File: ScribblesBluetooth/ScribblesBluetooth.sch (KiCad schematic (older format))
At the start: 9 parts

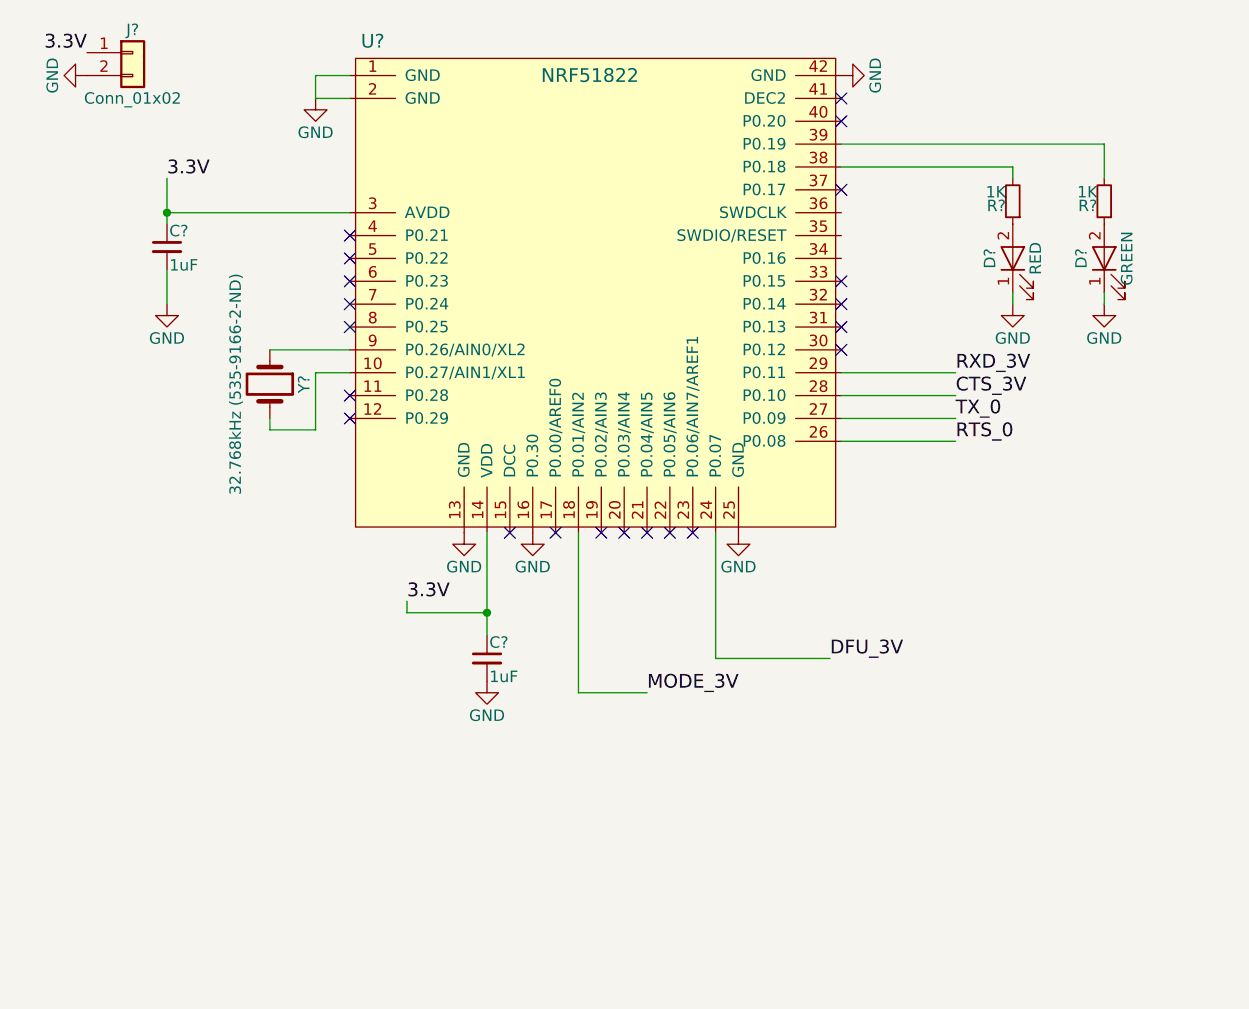
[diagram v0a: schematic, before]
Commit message: Finished bluetooth board
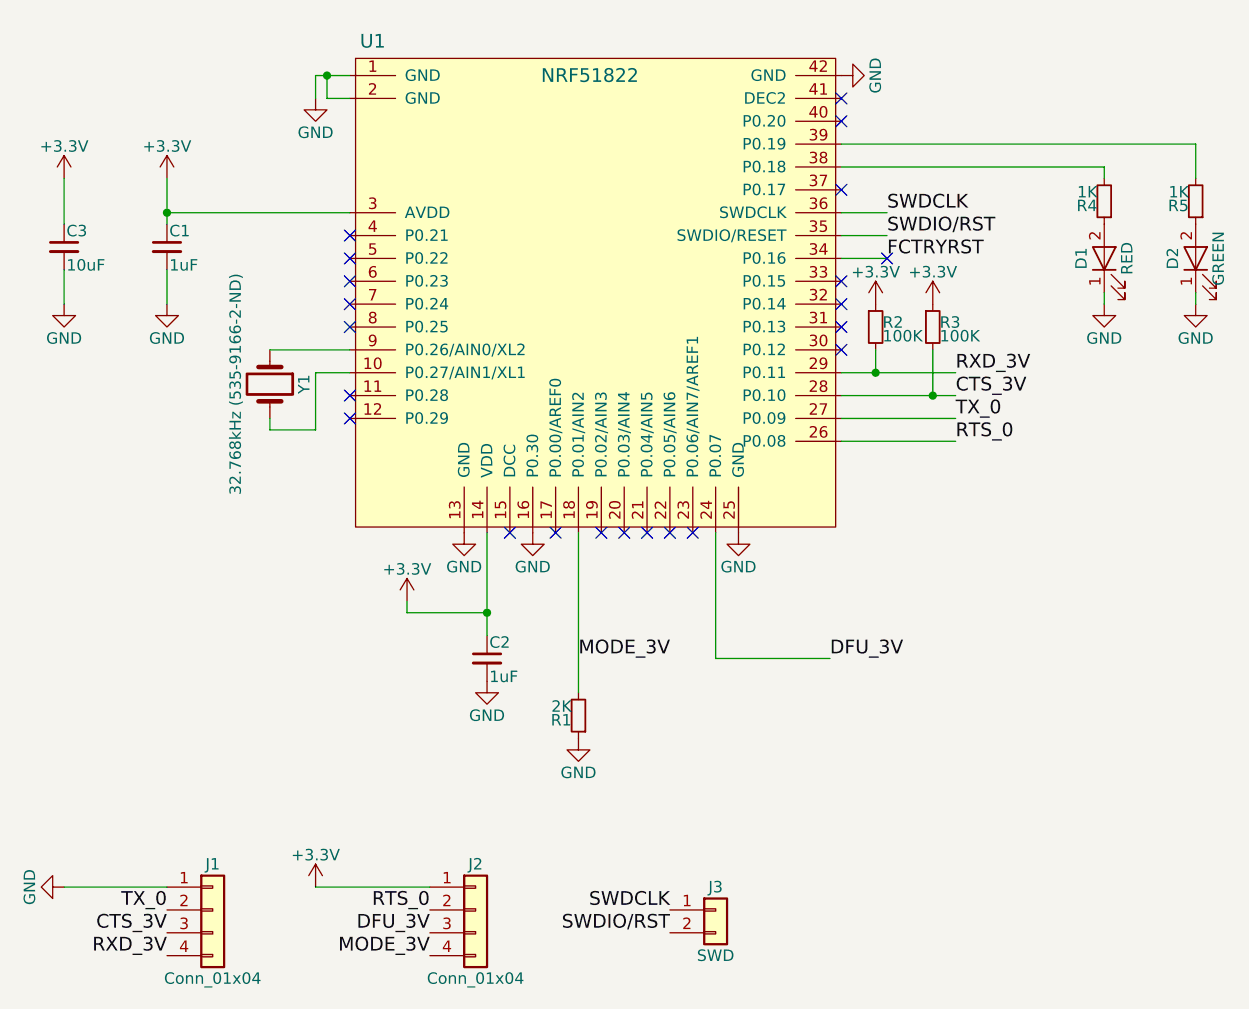
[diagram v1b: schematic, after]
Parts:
- removed J?: Conn_01x02, symbol Conn_01x02
- added C3: 10uF, Capacitors_SMD:C_0402, symbol C_Small
- added J1, J2: Conn_01x04, Pin_Headers:Pin_Header_Straight_1x04_Pitch2.54mm, symbol Conn_01x04
- added J3: SWD, Pin_Headers:Pin_Header_Straight_1x02_Pitch2.54mm, symbol Conn_01x02
- added R1: 2K, Resistors_SMD:R_0402, symbol R_Small
- added R2, R3: 100K, Resistors_SMD:R_0402, symbol R_Small
- C1, C2: renamed from C?; footprint (none) -> Capacitors_SMD:C_0402
- D1, D2: renamed from D?; footprint (none) -> LEDs:LED_0402
- R4, R5: renamed from R?; footprint (none) -> Resistors_SMD:R_0402
- U1: renamed from U?; footprint (none) -> lib_fp:NRF51822
- Y1: renamed from Y?; footprint (none) -> ECS-.327-12.5-34B-TR:XTAL320X150X90N
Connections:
- net CTS_3V: now also J1.3 (Pin_3), R3.2
- net DFU_3V: now also J2.3 (Pin_3)
- net GND: now also C3.2, J1.1 (Pin_1), R1.1
- net MODE_3V: now also J2.4 (Pin_4), R1.2
- net RTS_0: now also J2.2 (Pin_2)
- net RXD_3V: now also J1.4 (Pin_4), R2.2
- net TX_0: now also J1.2 (Pin_2)
- net FCTRYRST: now reaches U1.34 (P0.16)
- net SWDIO/RST: now reaches U1.35 (SWDIO/RESET)
- net SWDIO/RST: now also J3.2 (Pin_2)
- net SWDCLK: now reaches U1.36 (SWDCLK)
- net SWDCLK: now also J3.1 (Pin_1)
- net 3.3V renamed +3V3
- net +3V3: now also C3.1, J2.1 (Pin_1), R2.1, R3.1
- no-connect marks 21 -> 22
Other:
- moved on the sheet: D1, D2, R4, R5
